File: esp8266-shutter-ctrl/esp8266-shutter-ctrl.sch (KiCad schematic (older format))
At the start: 0 parts

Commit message: shutter-ctrl: sch: first try
Signed-off-by: Dominik Laton <dominik.laton@web.de>
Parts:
- added H1, H2, H3, H4: MountingHole, MountingHole:MountingHole_4.3mm_M4_ISO14580_Pad, symbol Mechanical:MountingHole
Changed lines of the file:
@@
 $Descr A4 11693 8268
 encoding utf-8
-Sheet 1 1
+Sheet 1 6
 Title "esp8266-shutter-ctrl"
 Date ""
@@
 Comment4 ""
 $EndDescr
+$Sheet
+S 5600 5600 900  300
+U 5FCBAC6B
+F0 "buttons" 50
+F1 "buttons.sch" 50
+F2 "shutter_button_int_a" O R 6500 5700 50
+F3 "shutter_button_int_b" O R 6500 5800 50
+$EndSheet
+$Sheet
+S 5700 3500 800  1800
+U 6015F217
+F0 "shutter" 50
+F1 "shutter.sch" 50
+F2 "shutter_0_up_out" O R 6500 3600 50
+F3 "shutter_1_up_out" O R 6500 3700 50
+F4 "shutter_2_up_out" O R 6500 3800 50
+F5 "shutter_3_up_out" O R 6500 3900 50
+F6 "shutter_4_up_out" O R 6500 4000 50
+F7 "shutter_5_up_out" O R 6500 4100 50
+F8 "shutter_6_up_out" O R 6500 4200 50
+F9 "shutter_en_+12V" O R 6500 5200 50
+F10 "shutter_0_dn_out" O R 6500 4400 50
+F11 "shutter_1_dn_out" O R 6500 4500 50
+F12 "shutter_2_dn_out" O R 6500 4600 50
+F13 "shutter_3_dn_out" O R 6500 4700 50
+F14 "shutter_4_dn_out" O R 6500 4800 50
+F15 "shutter_6_dn_out" O R 6500 5000 50
+F16 "shutter_5_dn_out" O R 6500 4900 50
+$EndSheet
+Wire Wire Line
+	6500 3600 7050 3600
+Wire Wire Line
+	6500 3700 7050 3700
+Wire Wire Line
+	6500 3800 7050 3800
+Wire Wire Line
+	6500 3900 7050 3900
+Wire Wire Line
+	6500 4000 7050 4000
+Wire Wire Line
+	6500 4100 7050 4100
+Wire Wire Line
+	6500 4200 7050 4200
+Wire Wire Line
+	6500 4400 7050 4400
+Wire Wire Line
+	6500 4500 7050 4500
+Wire Wire Line
+	6500 4600 7050 4600
+Wire Wire Line
+	6500 4700 7050 4700
+Wire Wire Line
+	6500 4800 7050 4800
+Wire Wire Line
+	6500 4900 7050 4900
+Wire Wire Line
+	6500 5000 7050 5000
+Wire Wire Line
+	6500 5200 7050 5200
+Wire Wire Line
+	6500 5700 6750 5700
+Wire Wire Line
+	6750 5700 6750 5400
+Wire Wire Line
+	6750 5400 7050 5400
+Wire Wire Line
+	6500 5800 6800 5800
+Wire Wire Line
+	6800 5800 6800 5500
+Wire Wire Line
+	6800 5500 7050 5500
+$Comp
+L Mechanical:MountingHole H2
+U 1 1 6022BCCB
+P 1750 4250
+F 0 "H2" H 1850 4296 50  0000 L CNN
+F 1 "MountingHole" H 1850 4205 50  0000 L CNN
+F 2 "MountingHole:MountingHole_4.3mm_M4_ISO14580_Pad" H 1750 4250 50  0001 C CNN
+F 3 "~" H 1750 4250 50  0001 C CNN
+	1    1750 4250
+	1    0    0    -1
+$EndComp
+$Comp
+L Mechanical:MountingHole H4
+U 1 1 6022BE3C
+P 2650 4250
+F 0 "H4" H 2750 4296 50  0000 L CNN
+F 1 "MountingHole" H 2750 4205 50  0000 L CNN
+F 2 "MountingHole:MountingHole_4.3mm_M4_ISO14580_Pad" H 2650 4250 50  0001 C CNN
+F 3 "~" H 2650 4250 50  0001 C CNN
+	1    2650 4250
+	1    0    0    -1
+$EndComp
+$Comp
+L Mechanical:MountingHole H3
+U 1 1 6022BF25
+P 2600 4700
+F 0 "H3" H 2700 4746 50  0000 L CNN
+F 1 "MountingHole" H 2700 4655 50  0000 L CNN
+F 2 "MountingHole:MountingHole_4.3mm_M4_ISO14580_Pad" H 2600 4700 50  0001 C CNN
+F 3 "~" H 2600 4700 50  0001 C CNN
+	1    2600 4700
+	1    0    0    -1
+$EndComp
+$Comp
+L Mechanical:MountingHole H1
+U 1 1 6022BFD2
+P 1650 4650
+F 0 "H1" H 1750 4696 50  0000 L CNN
+F 1 "MountingHole" H 1750 4605 50  0000 L CNN
+F 2 "MountingHole:MountingHole_4.3mm_M4_ISO14580_Pad" H 1650 4650 50  0001 C CNN
+F 3 "~" H 1650 4650 50  0001 C CNN
+	1    1650 4650
+	1    0    0    -1
+$EndComp
+$Sheet
+S 7050 3500 2750 2600
+U 5FCBAC93
+F0 "connectors" 50
+F1 "connectors.sch" 50
+F2 "shutter_0_up_out" I L 7050 3600 50
+F3 "shutter_1_up_out" I L 7050 3700 50
+F4 "shutter_2_up_out" I L 7050 3800 50
+F5 "shutter_3_up_out" I L 7050 3900 50
+F6 "shutter_4_up_out" I L 7050 4000 50
+F7 "shutter_5_up_out" I L 7050 4100 50
+F8 "shutter_6_up_out" I L 7050 4200 50
+F9 "shutter_0_dn_out" I L 7050 4400 50
+F10 "shutter_1_dn_out" I L 7050 4500 50
+F11 "shutter_2_dn_out" I L 7050 4600 50
+F12 "shutter_3_dn_out" I L 7050 4700 50
+F13 "shutter_4_dn_out" I L 7050 4800 50
+F14 "shutter_5_dn_out" I L 7050 4900 50
+F15 "shutter_6_dn_out" I L 7050 5000 50
+F16 "shutter_en_+12V" I L 7050 5200 50
+F17 "shutter_button_int_a" I L 7050 5400 50
+F18 "shutter_button_int_b" I L 7050 5500 50
+$EndSheet
+$Sheet
+S 7700 2350 500  150
+U 5FCBAC22
+F0 "power" 50
+F1 "power.sch" 50
+$EndSheet
 $EndSCHEMATC

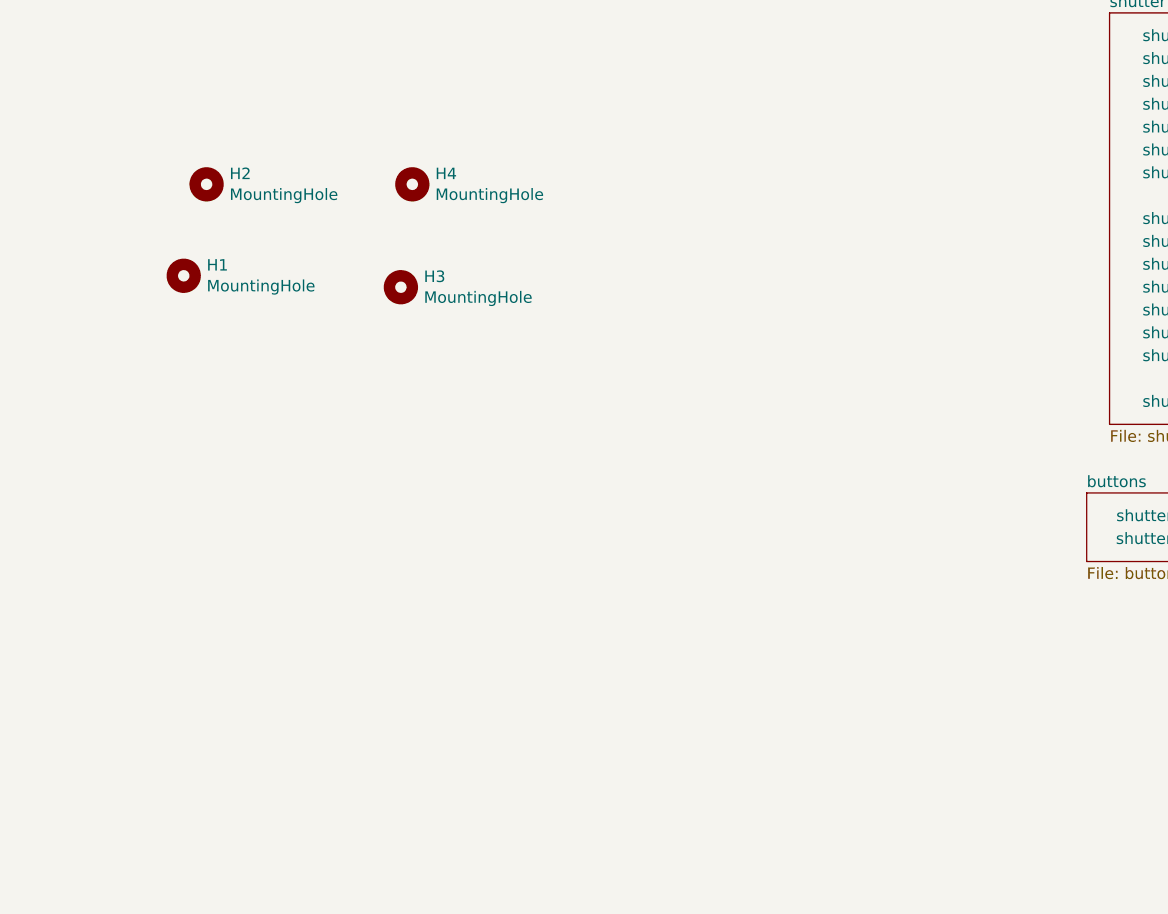
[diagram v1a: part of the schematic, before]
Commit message: shutter-ctrl: sch: added fuse and updated description
Signed-off-by: Dominik Laton <dominik.laton@web.de>
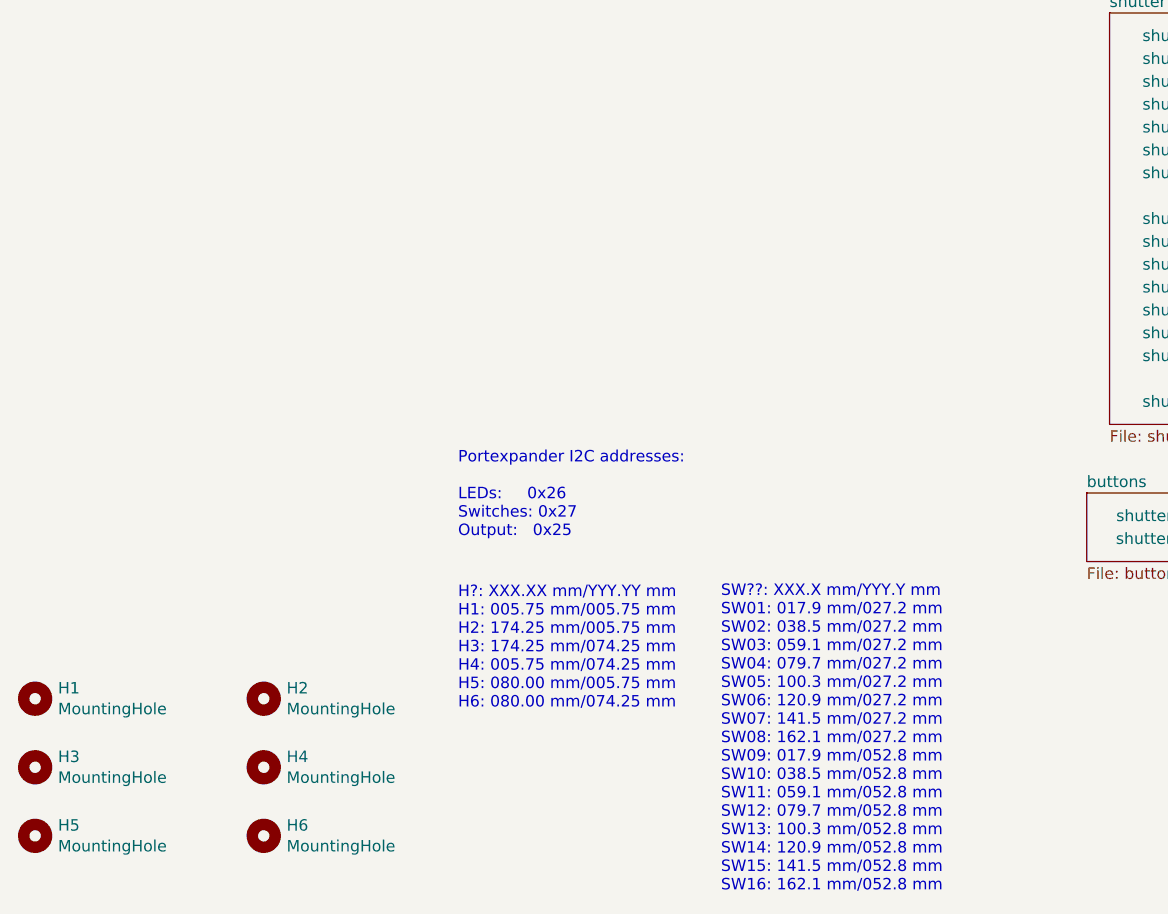
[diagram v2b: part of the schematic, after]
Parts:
- added H5, H6: MountingHole, MountingHole:MountingHole_4.3mm_M4_ISO14580_Pad, symbol Mechanical:MountingHole
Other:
- note added: "H?: XXX.XX mm/YYY.YY mm\nH1: 005.75 mm/005.75 mm\nH2: 174.25 mm/005.75 mm\nH3: 174.25 mm/074.25 mm\nH4: 005.75 mm/074.25 mm\nH5: 080.00 mm/005.75 mm\nH6: 080.00 mm/074.25 mm"
- note added: "Portexpander I2C addresses:\n\nLEDs: 0x26\nSwitches: 0x27\nOutput: 0x25"
- note added: "SW??: XXX.X mm/YYY.Y mm\nSW01: 017.9 mm/027.2 mm\nSW02: 038.5 mm/027.2 mm\nSW03: 059.1 mm/027.2 mm\nSW04: 079.7 mm/027.2 mm\nSW05: 100.3 mm/027.2 mm\nSW06: 120.9 mm/027.2 mm\nSW07: 141.5 mm/027.2 mm\nSW08: 162.1 mm/027.2 mm\nSW09: 017.9 mm/052.8 mm\nSW10: 038.5 mm/052.8 mm\nSW11: 059.1 mm/052.8 mm\nSW12: 079.7 mm/052.8 mm\nSW13: 100.3 mm/052.8 mm\nSW14: 120.9 mm/052.8 mm\nSW15: 141.5 mm/052.8 mm\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"
- moved on the sheet: H1, H2, H3, H4
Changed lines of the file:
@@
 L Mechanical:MountingHole H2
 U 1 1 6022BCCB
-P 1750 4250
-F 0 "H2" H 1850 4296 50  0000 L CNN
-F 1 "MountingHole" H 1850 4205 50  0000 L CNN
-F 2 "MountingHole:MountingHole_4.3mm_M4_ISO14580_Pad" H 1750 4250 50  0001 C CNN
-F 3 "~" H 1750 4250 50  0001 C CNN
-	1    1750 4250
+P 2000 6500
+F 0 "H2" H 2100 6546 50  0000 L CNN
+F 1 "MountingHole" H 2100 6455 50  0000 L CNN
+F 2 "MountingHole:MountingHole_4.3mm_M4_ISO14580_Pad" H 2000 6500 50  0001 C CNN
+F 3 "~" H 2000 6500 50  0001 C CNN
+	1    2000 6500
 	1    0    0    -1
 $EndComp
@@
 L Mechanical:MountingHole H4
 U 1 1 6022BE3C
-P 2650 4250
-F 0 "H4" H 2750 4296 50  0000 L CNN
-F 1 "MountingHole" H 2750 4205 50  0000 L CNN
-F 2 "MountingHole:MountingHole_4.3mm_M4_ISO14580_Pad" H 2650 4250 50  0001 C CNN
-F 3 "~" H 2650 4250 50  0001 C CNN
-	1    2650 4250
+P 2000 6800
+F 0 "H4" H 2100 6846 50  0000 L CNN
+F 1 "MountingHole" H 2100 6755 50  0000 L CNN
+F 2 "MountingHole:MountingHole_4.3mm_M4_ISO14580_Pad" H 2000 6800 50  0001 C CNN
+F 3 "~" H 2000 6800 50  0001 C CNN
+	1    2000 6800
 	1    0    0    -1
 $EndComp
@@
 L Mechanical:MountingHole H3
 U 1 1 6022BF25
-P 2600 4700
-F 0 "H3" H 2700 4746 50  0000 L CNN
-F 1 "MountingHole" H 2700 4655 50  0000 L CNN
-F 2 "MountingHole:MountingHole_4.3mm_M4_ISO14580_Pad" H 2600 4700 50  0001 C CNN
-F 3 "~" H 2600 4700 50  0001 C CNN
-	1    2600 4700
+P 1000 6800
+F 0 "H3" H 1100 6846 50  0000 L CNN
+F 1 "MountingHole" H 1100 6755 50  0000 L CNN
+F 2 "MountingHole:MountingHole_4.3mm_M4_ISO14580_Pad" H 1000 6800 50  0001 C CNN
+F 3 "~" H 1000 6800 50  0001 C CNN
+	1    1000 6800
 	1    0    0    -1
 $EndComp
@@
 L Mechanical:MountingHole H1
 U 1 1 6022BFD2
-P 1650 4650
-F 0 "H1" H 1750 4696 50  0000 L CNN
-F 1 "MountingHole" H 1750 4605 50  0000 L CNN
-F 2 "MountingHole:MountingHole_4.3mm_M4_ISO14580_Pad" H 1650 4650 50  0001 C CNN
-F 3 "~" H 1650 4650 50  0001 C CNN
-	1    1650 4650
+P 1000 6500
+F 0 "H1" H 1100 6546 50  0000 L CNN
+F 1 "MountingHole" H 1100 6455 50  0000 L CNN
+F 2 "MountingHole:MountingHole_4.3mm_M4_ISO14580_Pad" H 1000 6500 50  0001 C CNN
+F 3 "~" H 1000 6500 50  0001 C CNN
+	1    1000 6500
 	1    0    0    -1
 $EndComp
@@
 F1 "power.sch" 50
 $EndSheet
+$Comp
+L Mechanical:MountingHole H5
+U 1 1 5FCE119A
+P 1000 7100
+F 0 "H5" H 1100 7146 50  0000 L CNN
+F 1 "MountingHole" H 1100 7055 50  0000 L CNN
+F 2 "MountingHole:MountingHole_4.3mm_M4_ISO14580_Pad" H 1000 7100 50  0001 C CNN
+F 3 "~" H 1000 7100 50  0001 C CNN
+	1    1000 7100
+	1    0    0    -1
+$EndComp
+$Comp
+L Mechanical:MountingHole H6
+U 1 1 5FCE1374
+P 2000 7100
+F 0 "H6" H 2100 7146 50  0000 L CNN
+F 1 "MountingHole" H 2100 7055 50  0000 L CNN
+F 2 "MountingHole:MountingHole_4.3mm_M4_ISO14580_Pad" H 2000 7100 50  0001 C CNN
+F 3 "~" H 2000 7100 50  0001 C CNN
+	1    2000 7100
+	1    0    0    -1
+$EndComp
+Text Notes 2850 6550 0    50   ~ 0
+H?: XXX.XX mm/YYY.YY mm\nH1: 005.75 mm/005.75 mm\nH2: 174.25 mm/005.75 mm\nH3: 174.25 mm/074.25 mm\nH4: 005.75 mm/074.25 mm\nH5: 080.00 mm/005.75 mm\nH6: 080.00 mm/074.25 mm
+Text Notes 2850 5800 0    50   ~ 0
+Portexpander I2C addresses:\n\nLEDs:     0x26\nSwitches: 0x27\nOutput:   0x25
+Text Notes 4000 7350 0    50   ~ 0
+SW??: XXX.X mm/YYY.Y mm\nSW01: 017.9 mm/027.2 mm\nSW02: 038.5 mm/027.2 mm\nSW03: 059.1 mm/027.2 mm\nSW04: 079.7 mm/027.2 mm\nSW05: 100.3 mm/027.2 mm\nSW06: 120.9 mm/027.2 mm\nSW07: 141.5 mm/027.2 mm\nSW08: 162.1 mm/027.2 mm\nSW09: 017.9 mm/052.8 mm\nSW10: 038.5 mm/052.8 mm\nSW11: 059.1 mm/052.8 mm\nSW12: 079.7 mm/052.8 mm\nSW13: 100.3 mm/052.8 mm\nSW14: 120.9 mm/052.8 mm\nSW15: 141.5 mm/052.8 mm\nSW16: 162.1 mm/052.8 mm
 $EndSCHEMATC
